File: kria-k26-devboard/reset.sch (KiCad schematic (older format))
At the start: 27 parts, among them Q8 BSS138-7-F, U29 SN74AVC4T245PWR, U30 SN74AVC4T245PWR, U31 TPS3840PH30DBVR, U32 TPS3840PH30DBVR, U33 74LV07ATPWJ

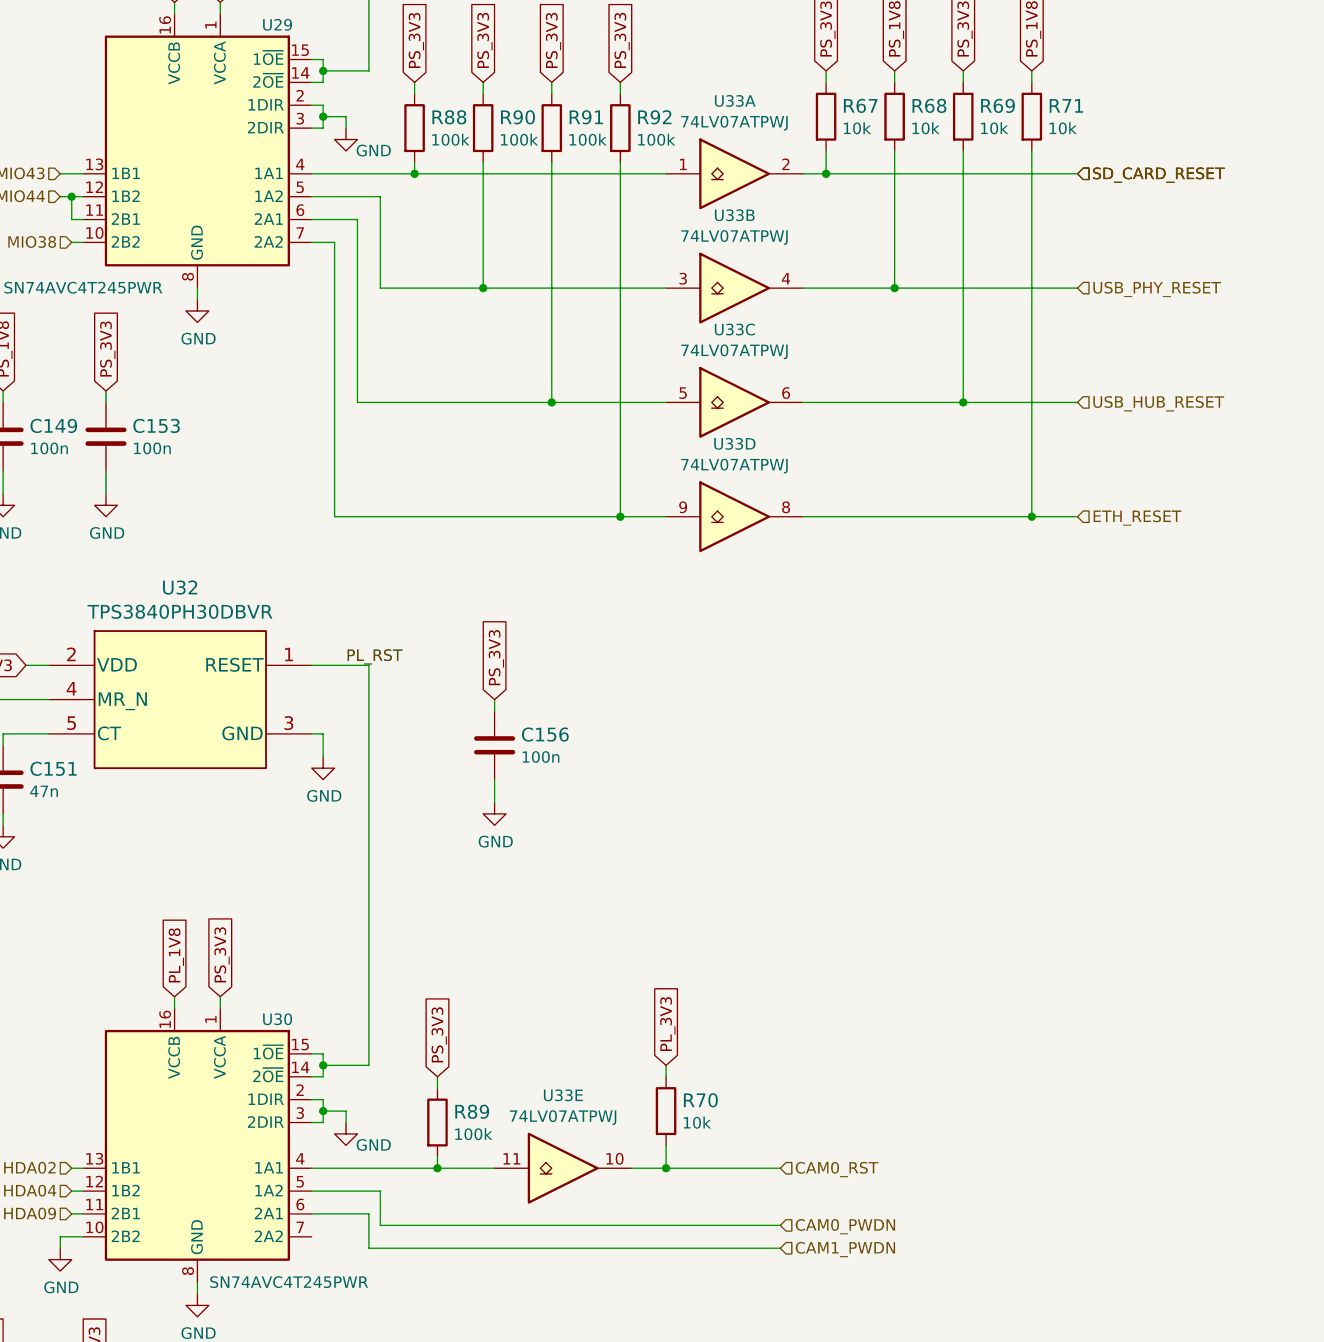
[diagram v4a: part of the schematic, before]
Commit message: Fixes on Reset pagae, progress through clock sheet
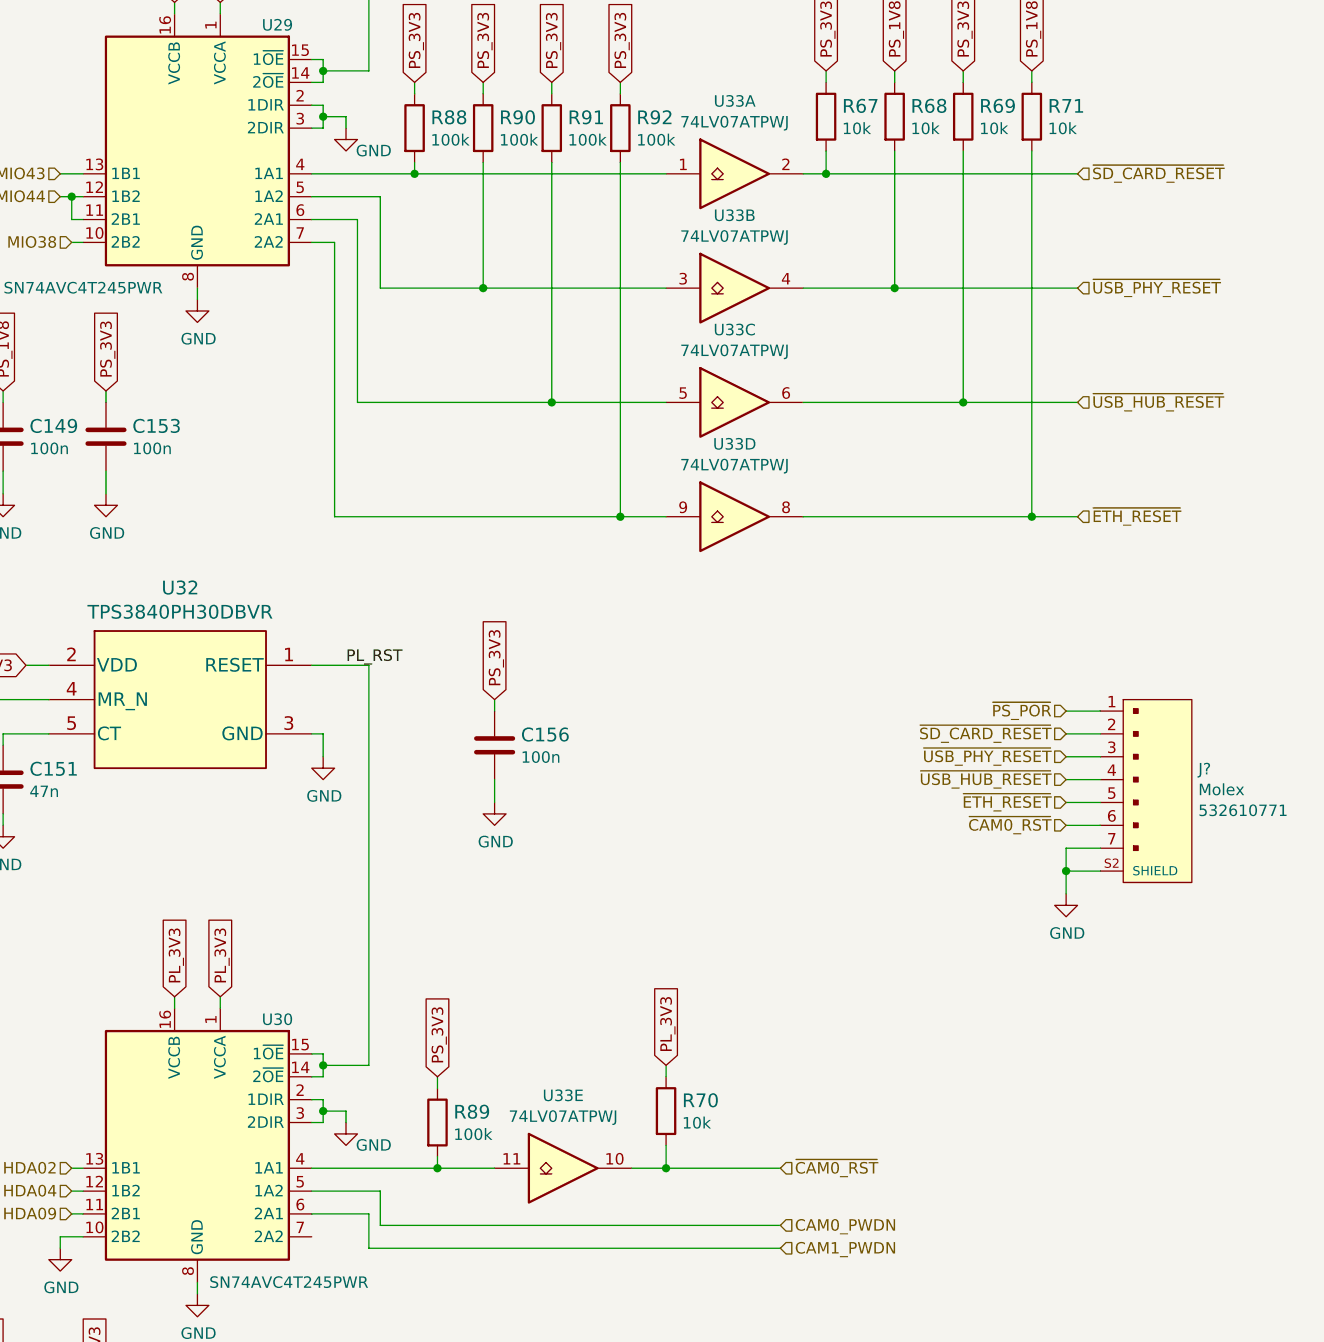
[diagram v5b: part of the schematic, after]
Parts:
- added J?: 532610771, antmicro-footprints:MOLEX_532610771, symbol antmicroRectangularConnectorsHeadersMalePins:532610771
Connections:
- net PL_1V8 is gone; now on net PL_3V3: U30.16 (VCCB)
- net GND: now also J?.7, J?.S1 (SHIELD), J?.S2 (SHIELD)
- net PL_3V3: now also U30.1 (VCCA)
- net PS_3V3: no longer U30.1 (VCCA)
- net ~PS_POR: now also J?.1
- net CAM0_RST renamed ~CAM0_RST
- net ~CAM0_RST: now also J?.6
- net ETH_RESET renamed ~ETH_RESET
- net ~ETH_RESET: now also J?.5
- net SD_CARD_RESET renamed ~SD_CARD_RESET
- net ~SD_CARD_RESET: now also J?.2
- net USB_HUB_RESET renamed ~USB_HUB_RESET
- net ~USB_HUB_RESET: now also J?.4
- net USB_PHY_RESET renamed ~USB_PHY_RESET
- net ~USB_PHY_RESET: now also J?.3
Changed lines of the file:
@@
 $Descr A3 16535 11693
 encoding utf-8
-Sheet 17 19
+Sheet 15 19
 Title ""
 Date ""
@@
 	11350 4850 11550 4850
 Connection ~ 11350 4850
-Text HLabel 11550 3350 2    50   Input ~ 0
-SD_CARD_RESET
 Text HLabel 11550 3850 2    50   Input ~ 0
-USB_PHY_RESET
+~USB_PHY_RESET
 Text HLabel 11550 4350 2    50   Input ~ 0
-USB_HUB_RESET
+~USB_HUB_RESET
 Text HLabel 11550 4850 2    50   Input ~ 0
-ETH_RESET
+~ETH_RESET
 Text GLabel 9450 9450 1    50   Input ~ 0
 SOM_5V
@@
 Wire Wire Line
 	7100 8000 7200 8000
-Text GLabel 7800 6950 1    50   Input ~ 0
-PS_3V3
-Text GLabel 7600 6950 1    50   Input ~ 0
-PL_1V8
 Wire Wire Line
 	8200 7800 8500 7800
@@
 MIO38
 Text HLabel 10250 7700 2    50   Input ~ 0
-CAM0_RST
+~CAM0_RST
 Text HLabel 10250 7950 2    50   Input ~ 0
 CAM0_PWDN
@@
 Wire Wire Line
 	10300 1200 10300 1050
-Text HLabel 11550 3350 2    50   Input ~ 0
-SD_CARD_RESET
 Text HLabel 10350 1050 2    50   Input ~ 0
 ~PS_POR
@@
 Text Notes 6300 6050 0    50   ~ 0
 25ms delay
+$Comp
+L antmicroRectangularConnectorsHeadersMalePins:532610771 J?
+U 1 1 6252DE32
+P 11750 6050
+F 0 "J?" H 12078 6146 50  0000 L CNN
+F 1 "532610771" H 11700 5550 50  0001 L BNN
+F 2 "antmicro-footprints:MOLEX_532610771" H 11750 6050 50  0001 L BNN
+F 3 "" H 11750 6050 50  0001 L BNN
+F 4 "Molex" H 12078 6055 50  0000 L CNN "Manufacturer"
+F 5 "532610771" H 12078 5964 50  0000 L CNN "MPN"
+	1    11750 6050
+	1    0    0    -1
+$EndComp
+Text HLabel 11500 5700 0    50   Input ~ 0
+~PS_POR
+$Comp
+L power:GND #PWR?
+U 1 1 6253AB9B
+P 11500 6500
+F 0 "#PWR?" H 11500 6250 50  0001 C CNN
+F 1 "GND" H 11505 6327 50  0000 C CNN
+F 2 "" H 11500 6500 50  0001 C CNN
+F 3 "" H 11500 6500 50  0001 C CNN
+	1    11500 6500
+	1    0    0    -1
+$EndComp
+Wire Wire Line
+	11650 6300 11500 6300
+Wire Wire Line
+	11500 6300 11500 6400
+Wire Wire Line
+	11650 6400 11500 6400
+Connection ~ 11500 6400
+Wire Wire Line
+	11500 6400 11500 6500
+Wire Wire Line
+	11500 5700 11650 5700
+Wire Wire Line
+	11650 5800 11500 5800
+Wire Wire Line
+	11500 5900 11650 5900
+Wire Wire Line
+	11650 6000 11500 6000
+Wire Wire Line
+	11500 6100 11650 6100
+Wire Wire Line
+	11650 6200 11500 6200
+Text HLabel 11550 3350 2    50   Input ~ 0
+~SD_CARD_RESET
+Text HLabel 11500 6200 0    50   Input ~ 0
+~CAM0_RST
+Text HLabel 11500 6100 0    50   Input ~ 0
+~ETH_RESET
+Text HLabel 11500 6000 0    50   Input ~ 0
+~USB_HUB_RESET
+Text HLabel 11500 5900 0    50   Input ~ 0
+~USB_PHY_RESET
+Text HLabel 11500 5800 0    50   Input ~ 0
+~SD_CARD_RESET
+Text GLabel 7600 6950 1    50   Input ~ 0
+PL_3V3
+Text GLabel 7800 6950 1    50   Input ~ 0
+PL_3V3
 $EndSCHEMATC

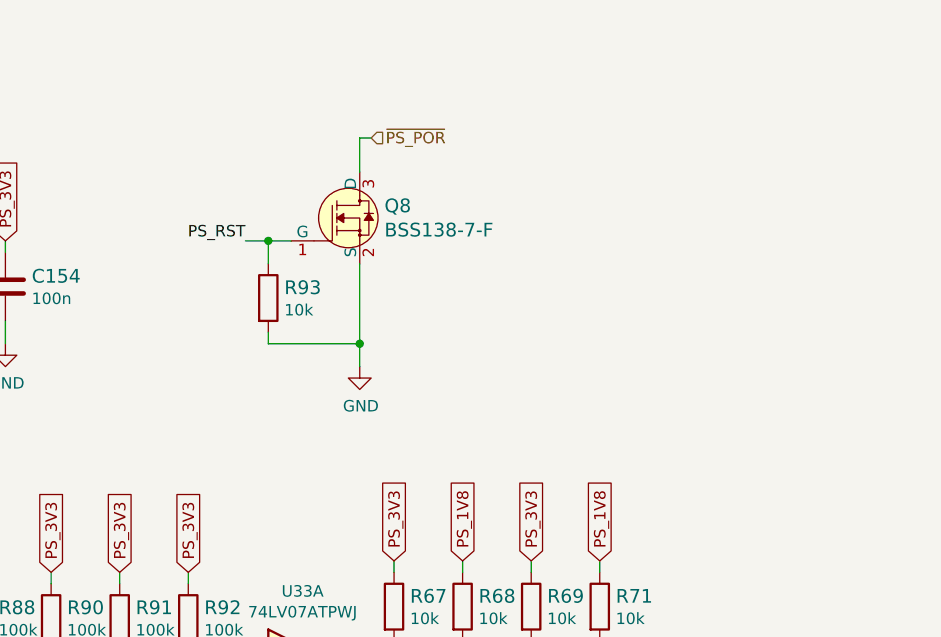
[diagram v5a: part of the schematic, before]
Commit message: Finished clock sheet
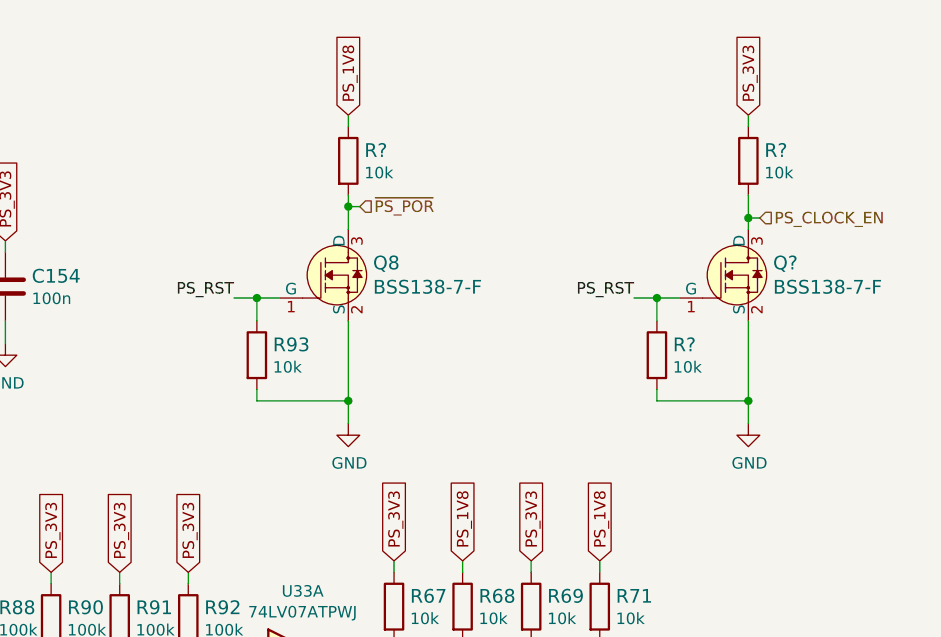
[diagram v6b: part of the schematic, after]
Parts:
- added Q?: BSS138-7-F, antmicro-footprints:SOT-23-3, symbol antmicroTransistorsFETsMOSFETsSingle:BSS138-7-F
- added R? (x3): R_10k_0402, antmicro-footprints:0402-res, symbol antmicroResistors0402:R_10k_0402
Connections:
- net GND: now also Q?.2 (S), R?.2
- net PS_1V8: now also R?.1
- net PS_3V3: now also R?.1
- net PS_RST: now also Q?.1 (G), R?.1
- net ~PS_POR: now also R?.2
- new net PS_CLOCK_EN: Q?.3 (D), R?.2
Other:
- moved on the sheet: Q8, R93
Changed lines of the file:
@@
 $Descr A3 16535 11693
 encoding utf-8
-Sheet 15 19
+Sheet 14 19
 Title ""
 Date ""
@@
 L antmicroTransistorsFETsMOSFETsSingle:BSS138-7-F Q8
 U 1 1 63E971C7
-P 10300 1400
-F 0 "Q8" H 10408 1453 60  0000 L CNN
-F 1 "BSS138-7-F" H 10408 1347 60  0000 L CNN
-F 2 "antmicro-footprints:SOT-23-3" H 10500 1600 60  0001 L CNN
-F 3 "https://www.diodes.com/assets/Datasheets/ds30144.pdf" H 10500 1700 60  0001 L CNN
-F 4 "BSS138-7-F" H 10500 1900 60  0001 L CNN "MPN"
-F 5 "Diodes Incorporated" H 10500 2500 60  0001 L CNN "Manufacturer"
-	1    10300 1400
+P 10250 1650
+F 0 "Q8" H 10358 1703 60  0000 L CNN
+F 1 "BSS138-7-F" H 10358 1597 60  0000 L CNN
+F 2 "antmicro-footprints:SOT-23-3" H 10450 1850 60  0001 L CNN
+F 3 "https://www.diodes.com/assets/Datasheets/ds30144.pdf" H 10450 1950 60  0001 L CNN
+F 4 "BSS138-7-F" H 10450 2150 60  0001 L CNN "MPN"
+F 5 "Diodes Incorporated" H 10450 2750 60  0001 L CNN "Manufacturer"
+	1    10250 1650
 	1    0    0    -1
 $EndComp
@@
 Text Label 8350 5500 0    50   ~ 0
 PL_RST
-Text Label 9800 1500 2    50   ~ 0
+Text Label 9750 1750 2    50   ~ 0
 PS_RST
 Wire Wire Line
-	9800 1500 9900 1500
+	9750 1750 9850 1750
 $Comp
 L power:GND #PWR0321
 U 1 1 63EA9D32
-P 10300 2050
-F 0 "#PWR0321" H 10300 1800 50  0001 C CNN
-F 1 "GND" H 10305 1877 50  0000 C CNN
-F 2 "" H 10300 2050 50  0001 C CNN
-F 3 "" H 10300 2050 50  0001 C CNN
-	1    10300 2050
+P 10250 2300
+F 0 "#PWR0321" H 10250 2050 50  0001 C CNN
+F 1 "GND" H 10255 2127 50  0000 C CNN
+F 2 "" H 10250 2300 50  0001 C CNN
+F 3 "" H 10250 2300 50  0001 C CNN
+	1    10250 2300
 	1    0    0    -1
 $EndComp
 Wire Wire Line
-	10300 1200 10300 1050
-Text HLabel 10350 1050 2    50   Input ~ 0
+	10250 1450 10250 1350
+Text HLabel 10300 1350 2    50   Input ~ 0
 ~PS_POR
 Wire Wire Line
-	10300 1050 10350 1050
+	10250 1350 10300 1350
 $Comp
 L antmicroResistors0402:R_10k_0402 R93
 U 1 1 63ED8AB3
-P 9900 1750
-F 0 "R93" V 9855 1820 60  0000 L CNN
-F 1 "R_10k_0402" H 9900 1600 60  0001 C CNN
-F 2 "antmicro-footprints:0402-res" H 10100 1950 60  0001 L CNN
-F 3 "" H 9900 1750 50  0001 C CNN
-F 4 "VISHAY" H 10100 2150 60  0001 L CNN "Manufacturer"
-F 5 "CRCW040210K0FKEDHP" H 10100 2050 60  0001 L CNN "MPN"
-F 6 "10k" V 9953 1820 50  0000 L CNN "Val"
-	1    9900 1750
+P 9850 2000
+F 0 "R93" V 9805 2070 60  0000 L CNN
+F 1 "R_10k_0402" H 9850 1850 60  0001 C CNN
+F 2 "antmicro-footprints:0402-res" H 10050 2200 60  0001 L CNN
+F 3 "" H 9850 2000 50  0001 C CNN
+F 4 "VISHAY" H 10050 2400 60  0001 L CNN "Manufacturer"
+F 5 "CRCW040210K0FKEDHP" H 10050 2300 60  0001 L CNN "MPN"
+F 6 "10k" V 9903 2070 50  0000 L CNN "Val"
+	1    9850 2000
 	0    1    1    0
 $EndComp
 Wire Wire Line
-	9900 1600 9900 1500
-Connection ~ 9900 1500
+	9850 1850 9850 1750
+Connection ~ 9850 1750
 Wire Wire Line
-	9900 1500 10000 1500
+	9850 1750 9950 1750
 Wire Wire Line
-	9900 1900 9900 1950
+	9850 2150 9850 2200
 Wire Wire Line
-	9900 1950 10300 1950
+	9850 2200 10250 2200
 Wire Wire Line
-	10300 1600 10300 1950
-Connection ~ 10300 1950
+	10250 1850 10250 2200
+Connection ~ 10250 2200
 Wire Wire Line
-	10300 1950 10300 2050
+	10250 2200 10250 2300
 Text GLabel 8650 2950 1    50   Input ~ 0
 PS_3V3
@@
 Text GLabel 7800 6950 1    50   Input ~ 0
 PL_3V3
+$Comp
+L antmicroTransistorsFETsMOSFETsSingle:BSS138-7-F Q?
+U 1 1 625BE7A7
+P 12000 1650
+F 0 "Q?" H 12108 1703 60  0000 L CNN
+F 1 "BSS138-7-F" H 12108 1597 60  0000 L CNN
+F 2 "antmicro-footprints:SOT-23-3" H 12200 1850 60  0001 L CNN
+F 3 "https://www.diodes.com/assets/Datasheets/ds30144.pdf" H 12200 1950 60  0001 L CNN
+F 4 "BSS138-7-F" H 12200 2150 60  0001 L CNN "MPN"
+F 5 "Diodes Incorporated" H 12200 2750 60  0001 L CNN "Manufacturer"
+	1    12000 1650
+	1    0    0    -1
+$EndComp
+Text Label 11500 1750 2    50   ~ 0
+PS_RST
+Wire Wire Line
+	11500 1750 11600 1750
+$Comp
+L power:GND #PWR?
+U 1 1 625BEA6D
+P 12000 2300
+F 0 "#PWR?" H 12000 2050 50  0001 C CNN
+F 1 "GND" H 12005 2127 50  0000 C CNN
+F 2 "" H 12000 2300 50  0001 C CNN
+F 3 "" H 12000 2300 50  0001 C CNN
+	1    12000 2300
+	1    0    0    -1
+$EndComp
+Wire Wire Line
+	12000 1450 12000 1400
+Text HLabel 12050 1400 2    50   Input ~ 0
+PS_CLOCK_EN
+$Comp
+L antmicroResistors0402:R_10k_0402 R?
+U 1 1 625BEA7D
+P 11600 2000
+F 0 "R?" V 11555 2070 60  0000 L CNN
+F 1 "R_10k_0402" H 11600 1850 60  0001 C CNN
+F 2 "antmicro-footprints:0402-res" H 11800 2200 60  0001 L CNN
+F 3 "" H 11600 2000 50  0001 C CNN
+F 4 "VISHAY" H 11800 2400 60  0001 L CNN "Manufacturer"
+F 5 "CRCW040210K0FKEDHP" H 11800 2300 60  0001 L CNN "MPN"
+F 6 "10k" V 11653 2070 50  0000 L CNN "Val"
+	1    11600 2000
+	0    1    1    0
+$EndComp
+Wire Wire Line
+	11600 1850 11600 1750
+Connection ~ 11600 1750
+Wire Wire Line
+	11600 1750 11700 1750
+Wire Wire Line
+	11600 2150 11600 2200
+Wire Wire Line
+	11600 2200 12000 2200
+Wire Wire Line
+	12000 1850 12000 2200
+Connection ~ 12000 2200
+Wire Wire Line
+	12000 2200 12000 2300
+Wire Wire Line
+	12050 1400 12000 1400
+Connection ~ 12000 1400
+Wire Wire Line
+	12000 1300 12000 1400
+Wire Wire Line
+	12000 1000 12000 950
+$Comp
+L antmicroResistors0402:R_10k_0402 R?
+U 1 1 625CF94D
+P 12000 1150
+F 0 "R?" V 11955 1220 60  0000 L CNN
+F 1 "R_10k_0402" H 12000 1000 60  0001 C CNN
+F 2 "antmicro-footprints:0402-res" H 12200 1350 60  0001 L CNN
+F 3 "" H 12000 1150 50  0001 C CNN
+F 4 "VISHAY" H 12200 1550 60  0001 L CNN "Manufacturer"
+F 5 "CRCW040210K0FKEDHP" H 12200 1450 60  0001 L CNN "MPN"
+F 6 "10k" V 12053 1220 50  0000 L CNN "Val"
+	1    12000 1150
+	0    1    1    0
+$EndComp
+Text GLabel 12000 950  1    50   Input ~ 0
+PS_3V3
+Text GLabel 10250 950  1    50   Input ~ 0
+PS_1V8
+$Comp
+L antmicroResistors0402:R_10k_0402 R?
+U 1 1 62627E6D
+P 10250 1150
+F 0 "R?" V 10205 1220 60  0000 L CNN
+F 1 "R_10k_0402" H 10250 1000 60  0001 C CNN
+F 2 "antmicro-footprints:0402-res" H 10450 1350 60  0001 L CNN
+F 3 "" H 10250 1150 50  0001 C CNN
+F 4 "VISHAY" H 10450 1550 60  0001 L CNN "Manufacturer"
+F 5 "CRCW040210K0FKEDHP" H 10450 1450 60  0001 L CNN "MPN"
+F 6 "10k" V 10303 1220 50  0000 L CNN "Val"
+	1    10250 1150
+	0    1    1    0
+$EndComp
+Wire Wire Line
+	10250 1000 10250 950
+Connection ~ 10250 1350
+Wire Wire Line
+	10250 1350 10250 1300
 $EndSCHEMATC
